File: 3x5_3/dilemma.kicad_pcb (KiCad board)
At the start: 2 copper layers, 134.1 x 215.7 mm, 82 parts, among them J5001 BATTERY_CONN_DEANS, J5011 BATTERY_CONN_DEANS, SW101 NA_SW_Push, SW102 NA_SW_Push, SW103 NA_SW_Push, SW104 NA_SW_Push, SW105 NA_SW_Push, SW106 NA_SW_Push, SW107 NA_SW_Push, SW108 NA_SW_Push, SW109 NA_SW_Push, SW112 NA_SW_Push, SW113 NA_SW_Push, SW114 NA_SW_Push, SW115 NA_SW_Push, SW116 NA_SW_Push, SW117 NA_SW_Push, SW118 NA_SW_Push, SW119 NA_SW_Push, SW3001 NA_SW_Push, SW5002 NA_SW_Push, SW5003 NA_SW_Push, SW5004 NA_SW_Push, SW5005 NA_SW_Push, SW5006 NA_SW_Push, SW5007 NA_SW_Push, SW5008 NA_SW_Push, SW5009 NA_SW_Push, SW5010 NA_SW_Push, SW5011 NA_SW_Push, SW5012 NA_SW_Push, SW5013 NA_SW_Push, SW5014 NA_SW_Push, SW5015 NA_SW_Push, SW5016 NA_SW_Push, SW5017 NA_SW_Push, SW5018 NA_SW_Push, SW5019 NA_SW_Push, SW5021 SW_SPST, SW5022 SW_SPST, U5001 eliteC, U5007 eliteC

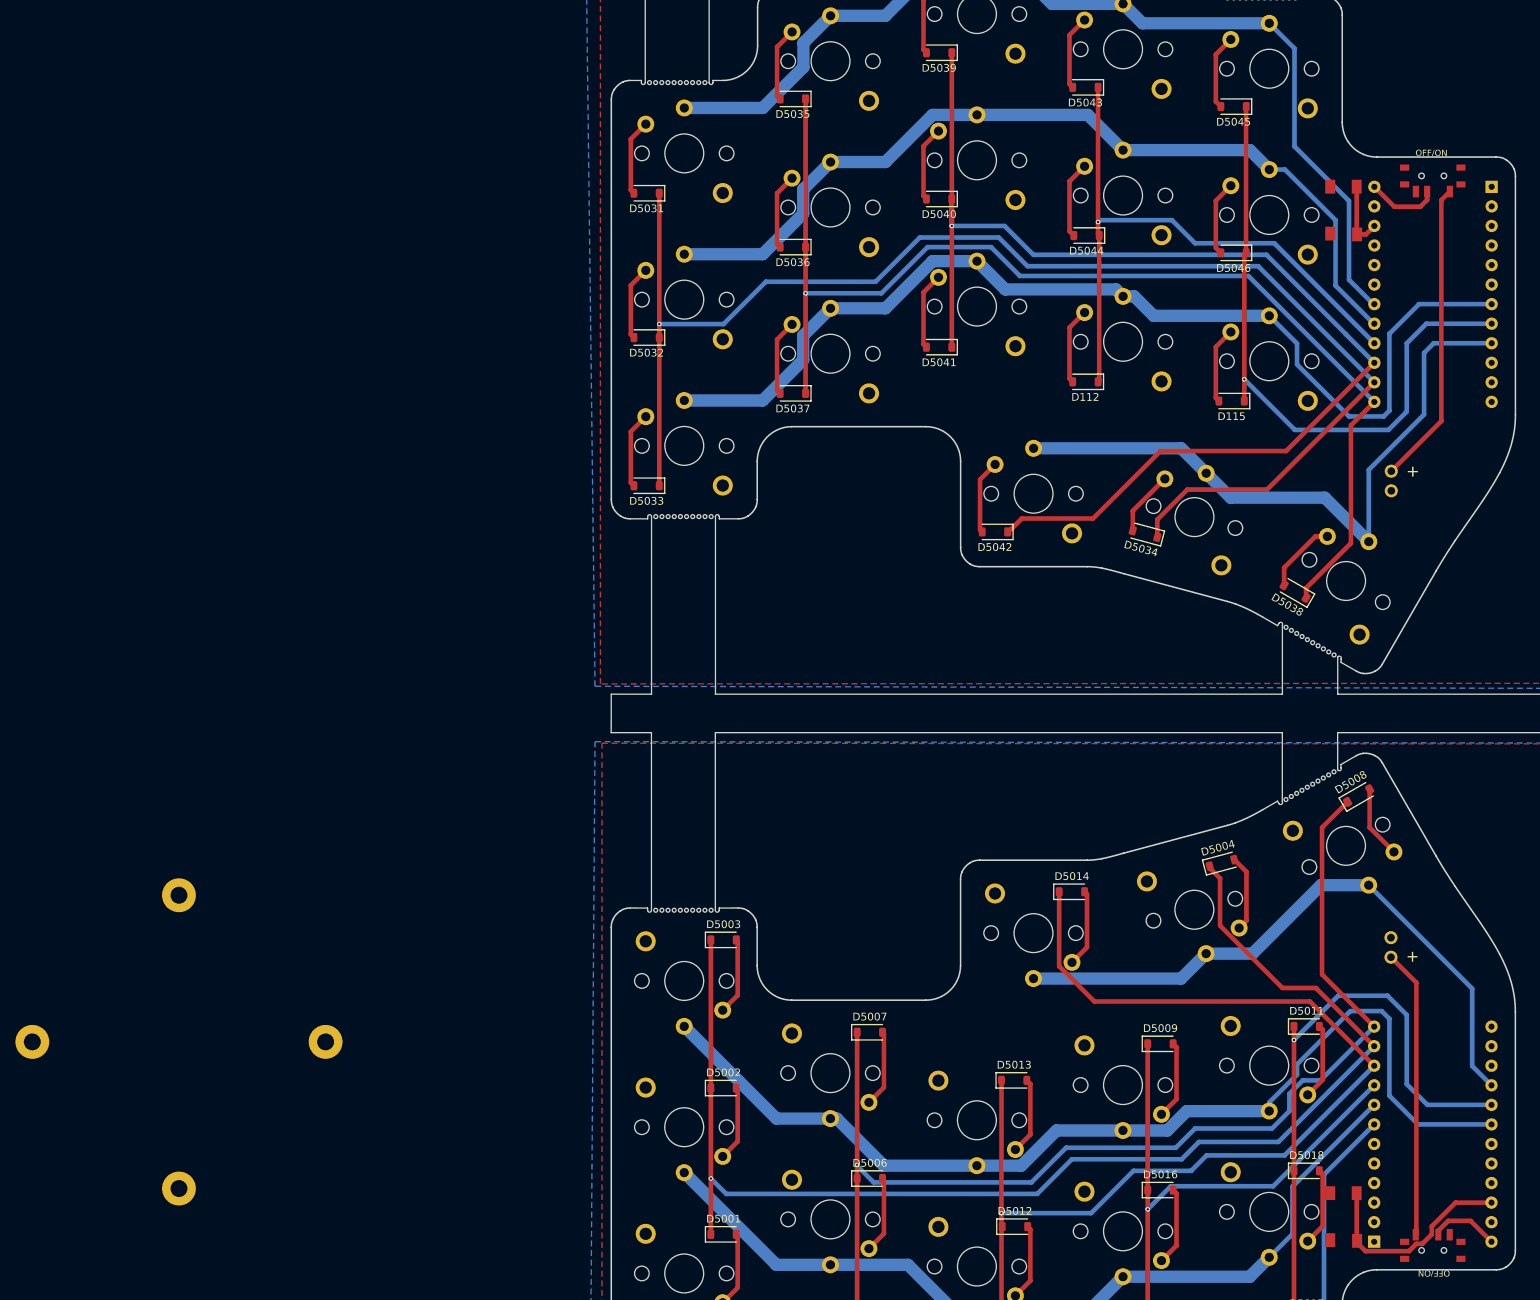
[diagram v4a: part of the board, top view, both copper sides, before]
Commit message: add right mounting holes
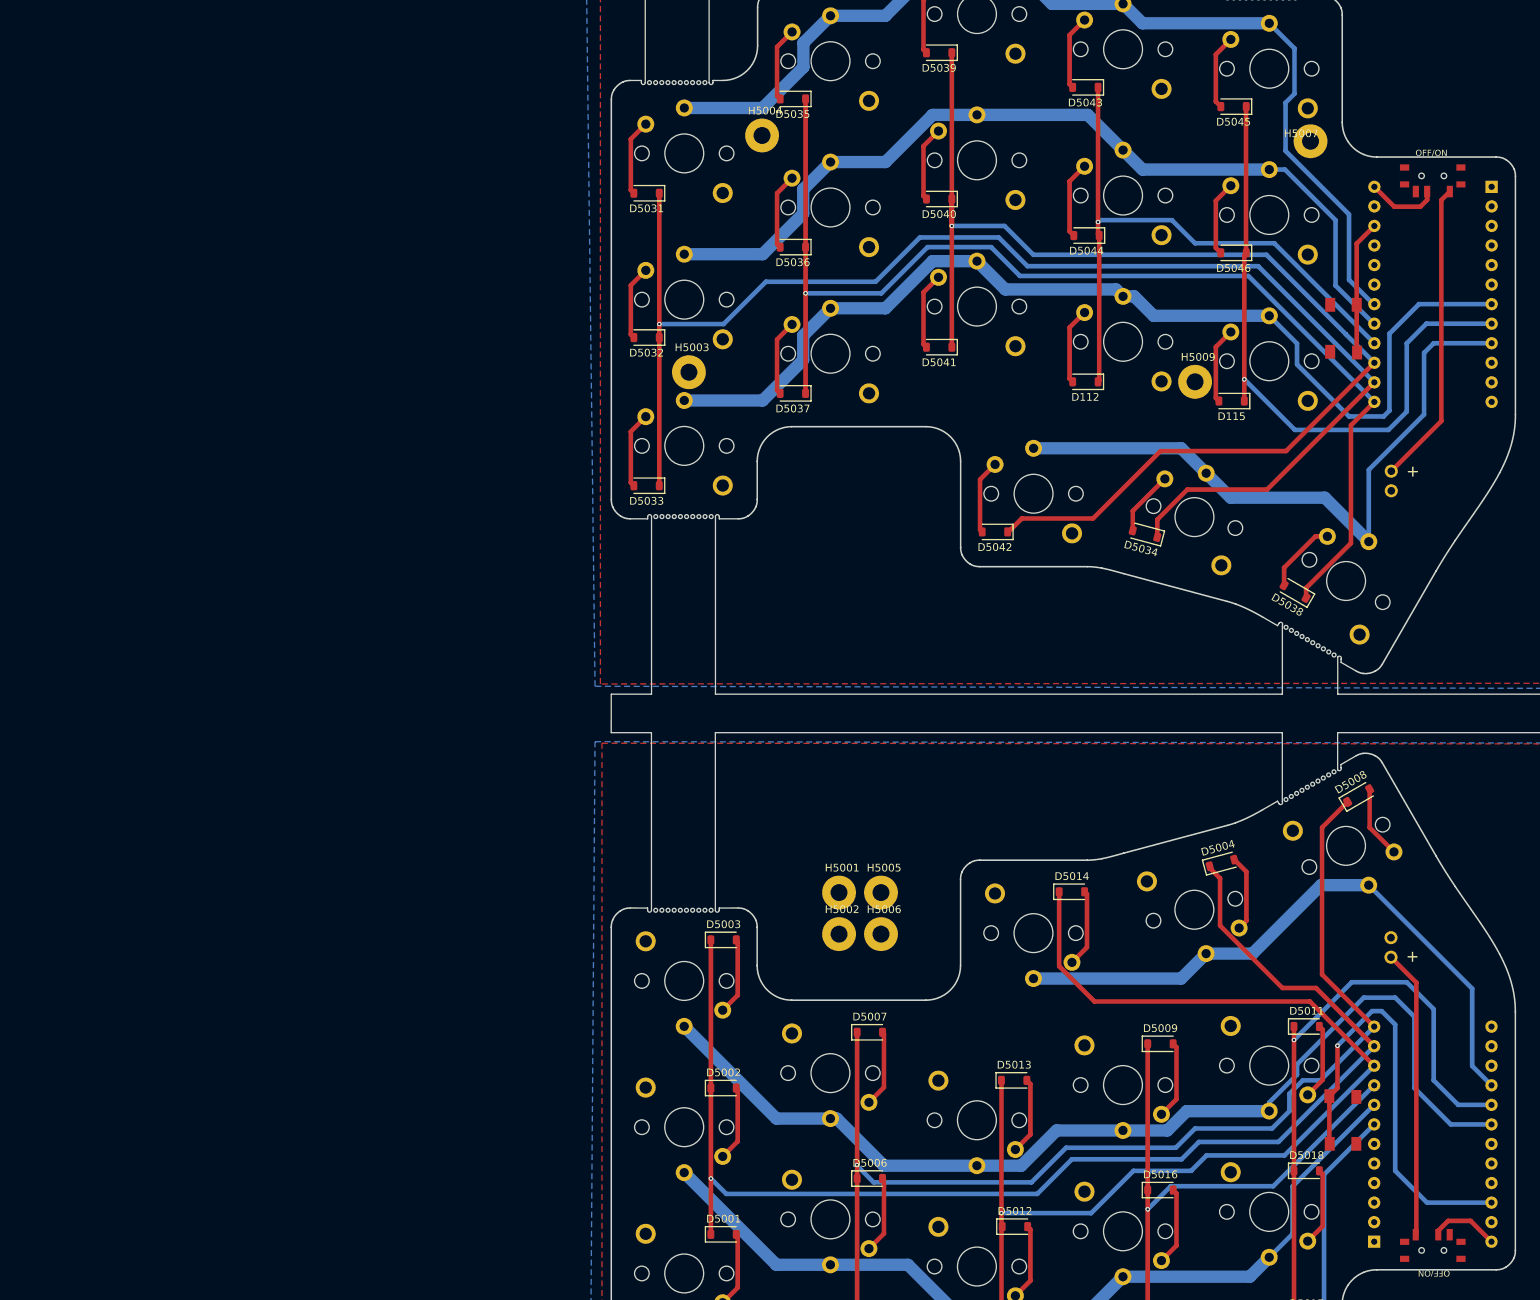
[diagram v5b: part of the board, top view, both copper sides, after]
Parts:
- removed H5008: NA_Mount, local-libraries:Tenting_Puck
- added H5001: NA_Mount, local-libraries:M2_Mounting_Hole, F.Cu at (142.0, 149.8)
- added H5002: NA_Mount, local-libraries:M2_Mounting_Hole, F.Cu at (142.0, 155.2)
- added H5003: NA_Mount, local-libraries:M2_Mounting_Hole, F.Cu at (122.5, 82.2)
- added H5004: NA_Mount, local-libraries:M2_Mounting_Hole, F.Cu at (132.0, 51.4)
- added H5005: NA_Mount, local-libraries:M2_Mounting_Hole, F.Cu at (147.4, 149.8)
- added H5006: NA_Mount, local-libraries:M2_Mounting_Hole, F.Cu at (147.4, 155.2)
- added H5007: NA_Mount, local-libraries:M2_Mounting_Hole, F.Cu at (201.6, 54.4)
- added H5009: NA_Mount, local-libraries:M2_Mounting_Hole, F.Cu at (188.2, 83.4)
- moved SW5022 15.3 mm to (207.5, 76.5)
- moved SW5021 12.6 mm to (207.5, 179.3), turned to 90 degrees
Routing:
- net RESET_L: track 27.6 -> 56.5 mm, vias 0 -> 1
- net RESET: track 8.92 -> 17.4 mm
- net M_COL5_L: track 77.2 -> 78.8 mm
- net M_ROW4_L: track 134.1 -> 135.1 mm
- net M_ROW2: track 130.5 -> 131.5 mm

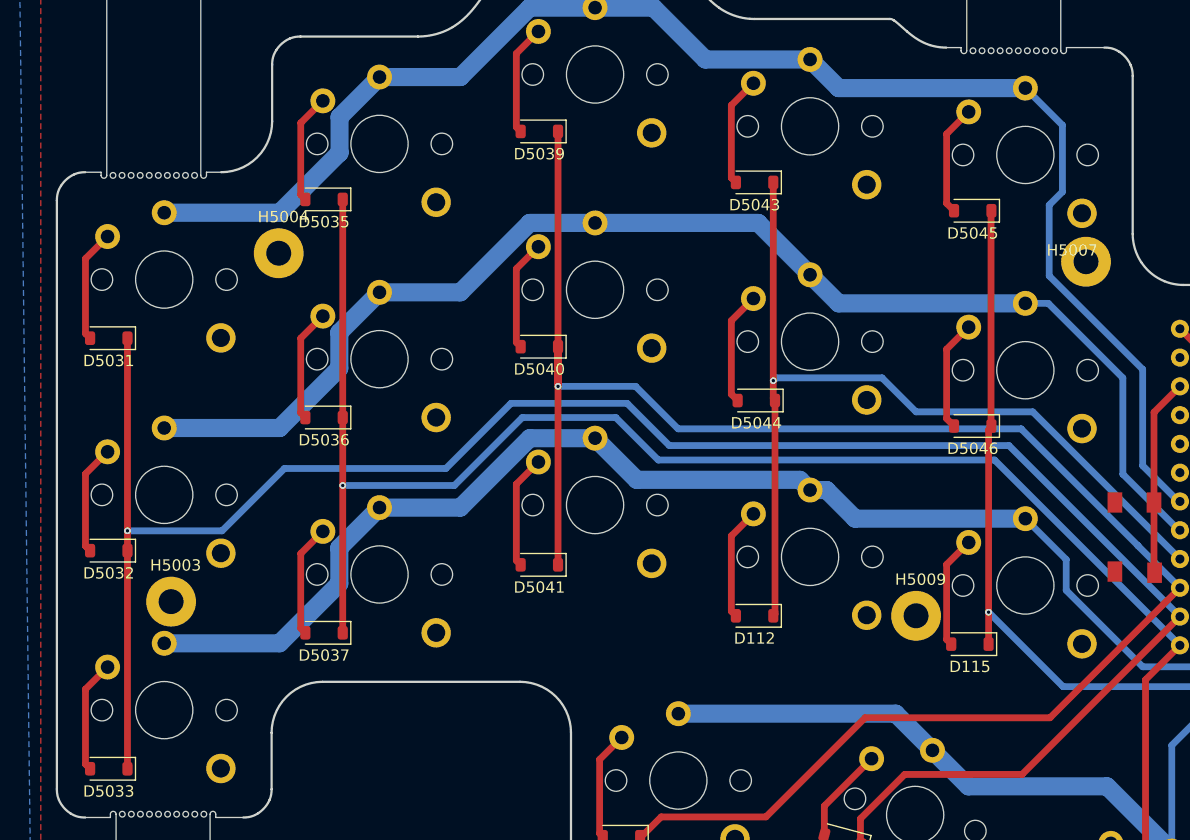
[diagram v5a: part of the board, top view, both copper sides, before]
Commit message: fix lower right mounting hole
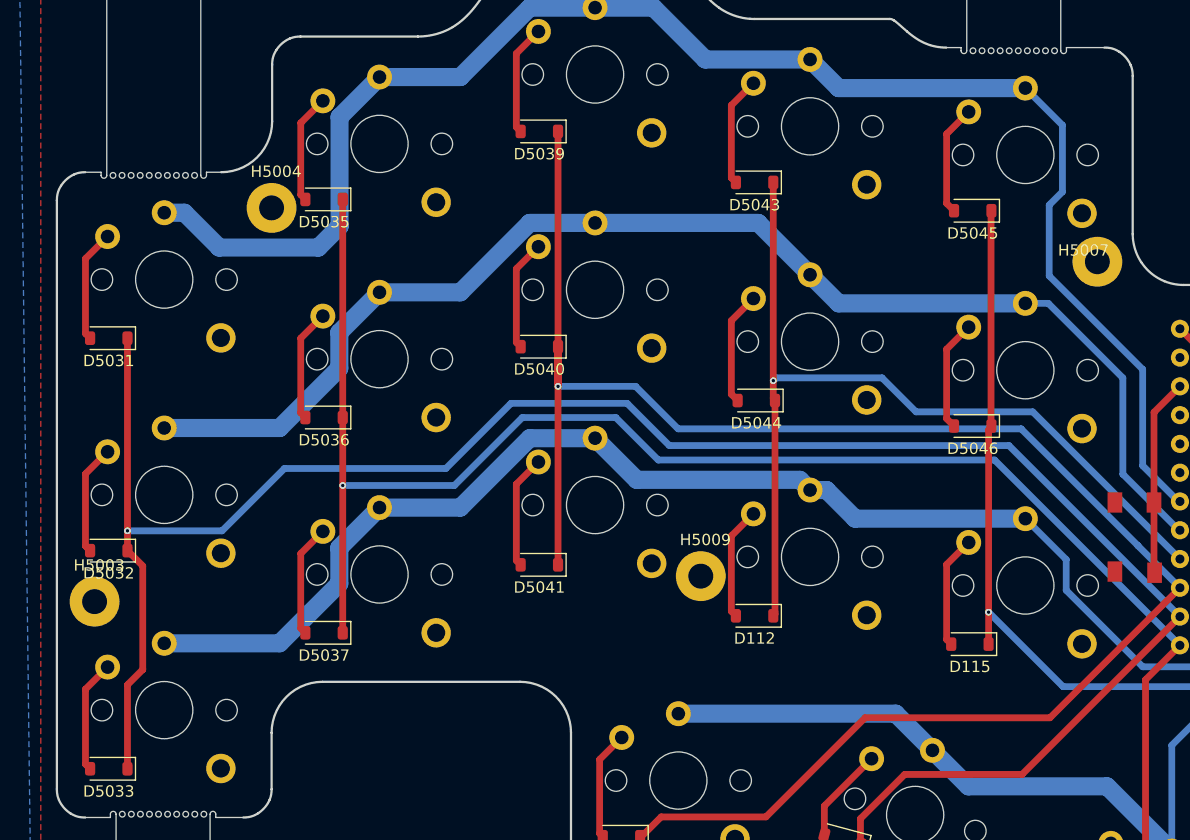
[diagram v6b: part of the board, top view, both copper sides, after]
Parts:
- moved H5009 19.3 mm to (169.2, 79.9)
- moved H5003 6.75 mm to (115.7, 82.2)
- moved H5004 4.05 mm to (131.3, 47.4)
- moved H5007 1.00 mm to (202.6, 54.4)
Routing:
- net M_ROW2: track 131.5 -> 137.8 mm
- net M_COL1: track 181.2 -> 182.3 mm
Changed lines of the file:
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@@
 	(footprint "local-libraries:M2_Mounting_Hole"
 		(layer "F.Cu")
-		(at 188.218798 83.421819)
+		(at 169.218798 79.921819)
 		(property "Reference" "H5009"
 			(at 0.4 -3.2 0)
@@
 	(footprint "local-libraries:M2_Mounting_Hole"
 		(layer "F.Cu")
-		(at 201.598796 54.371838)
+		(at 202.598796 54.371838)
 		(property "Reference" "H5007"
 			(at 0.4 -3.2 0)
@@
 		(fp_line
 			(start -0.35 0)
-			(end -0.35 -0.550001)
+			(end -0.35 -0.550002)
 			(stroke
 				(width 0.1)
@@
 	(footprint "local-libraries:M2_Mounting_Hole"
 		(layer "F.Cu")
-		(at 131.968798 51.421819)
+		(at 131.338798 47.421819)
 		(property "Reference" "H5004"
 			(at 0.4 -3.2 0)
@@
 	(footprint "local-libraries:M2_Mounting_Hole"
 		(layer "F.Cu")
-		(at 122.468798 82.171819)
+		(at 115.718798 82.171819)
 		(property "Reference" "H5003"
 			(at 0.4 -3.2 0)
@@
 	)
 	(segment
+		(start 119.968798 79.021819)
+		(end 119.968798 88.171819)
+		(width 0.6)
+		(layer "F.Cu")
+		(net 2)
+	)
+	(segment
 		(start 118.618798 58.921819)
 		(end 118.618798 75.921819)
@@
 	(segment
 		(start 118.618798 77.671819)
-		(end 118.618798 96.921819)
+		(end 119.968798 79.021819)
+		(width 0.6)
+		(layer "F.Cu")
+		(net 2)
+	)
+	(segment
+		(start 119.968798 88.171819)
+		(end 118.618798 89.521819)
 		(width 0.6)
 		(layer "F.Cu")
@@
 	)
 	(segment
+		(start 118.618798 89.521819)
+		(end 118.618798 96.921819)
+		(width 0.6)
+		(layer "F.Cu")
+		(net 2)
+	)
+	(segment
 		(start 197.577798 97.421819)
 		(end 211.508798 83.490819)
@@
 	)
 	(segment
-		(start 132.046524 47.8475)
-		(end 137.338808 42.555216)
-		(width 1.6)
-		(layer "B.Cu")
-		(net 9)
-	)
-	(segment
 		(start 208.218798 70.171819)
 		(end 211.377798 73.330819)
@@
 	)
 	(segment
+		(start 126.718798 50.921819)
+		(end 123.644479 47.8475)
+		(width 1.6)
+		(layer "B.Cu")
+		(net 9)
+	)
+	(segment
+		(start 140.863808 35.8725)
+		(end 137.338808 39.3975)
+		(width 1.6)
+		(layer "B.Cu")
+		(net 9)
+	)
+	(segment
 		(start 208.218798 61.671819)
 		(end 208.218798 70.171819)
@@
 	)
 	(segment
-		(start 137.338808 39.3975)
-		(end 140.863808 35.8725)
+		(start 123.644479 47.8475)
+		(end 121.863808 47.8475)
+		(width 1.6)
+		(layer "B.Cu")
+		(net 9)
+	)
+	(segment
+		(start 137.338808 49.051809)
+		(end 135.468798 50.921819)
 		(width 1.6)
 		(layer "B.Cu")
@@
 	)
 	(segment
-		(start 137.338808 42.555216)
-		(end 137.338808 39.3975)
+		(start 135.468798 50.921819)
+		(end 126.718798 50.921819)
 		(width 1.6)
 		(layer "B.Cu")
@@
 	)
 	(segment
+		(start 137.338808 39.3975)
+		(end 137.338808 49.051809)
+		(width 1.6)
+		(layer "B.Cu")
+		(net 9)
+	)
+	(segment
 		(start 154.122197 29.7475)
 		(end 159.888808 29.7475)
@@
 	)
 	(segment
-		(start 121.863808 47.8475)
-		(end 132.046524 47.8475)
-		(width 1.6)
-		(layer "B.Cu")
-		(net 9)
-	)
-	(segment
 		(start 140.863808 35.8725)
 		(end 147.997197 35.8725)
@@
 	)
 	(segment
-		(start 190.913808 78.8975)
-		(end 190.913808 85.516829)
+		(start 192.863808 76.9475)
+		(end 190.913808 78.8975)
 		(width 0.6)
 		(layer "F.Cu")
@@
 	)
 	(segment
-		(start 192.863808 76.9475)
-		(end 190.913808 78.8975)
+		(start 190.913808 78.8975)
+		(end 190.913808 85.516829)
 		(width 0.6)
 		(layer "F.Cu")
